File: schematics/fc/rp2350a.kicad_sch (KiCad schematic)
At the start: 53 parts, among them Q1 DMN1150UFB-7B, Q2 DMN1150UFB-7B, Q3 DMN1150UFB-7B, U2 TS2306A 240GF MSM 9_C2976675, U3 RP2354B_C39843328, X1 XTM25012000JT00351001

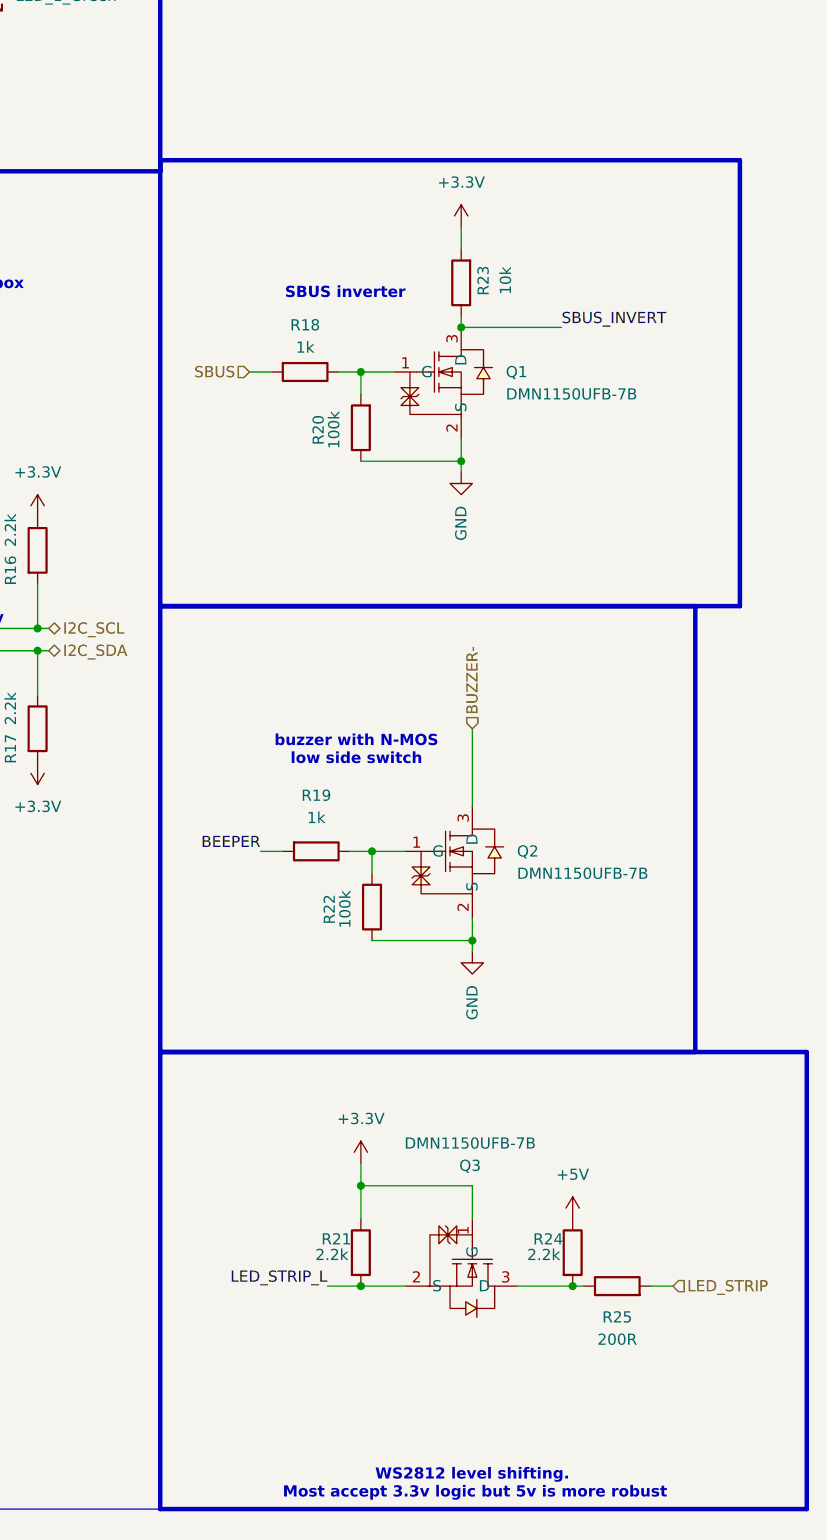
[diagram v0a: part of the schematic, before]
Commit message: checkpoint: Bluejay/BLHeli_S part imports + ESC rework notes
EFM8BB51F16G (C6547511), AGM310MAP (C5184858), BY25Q64ESCIG (C50176394)
imported into libs/lib.kicad_sym + lib.pretty + lib.3dshapes.
BLHELI_S_ESC_NOTES.md documents gate-drive research (1S direct drive vs
2S level-shift requirement) and open design decisions.

Co-Authored-By: Claude Fable 5 <noreply@anthropic.com>
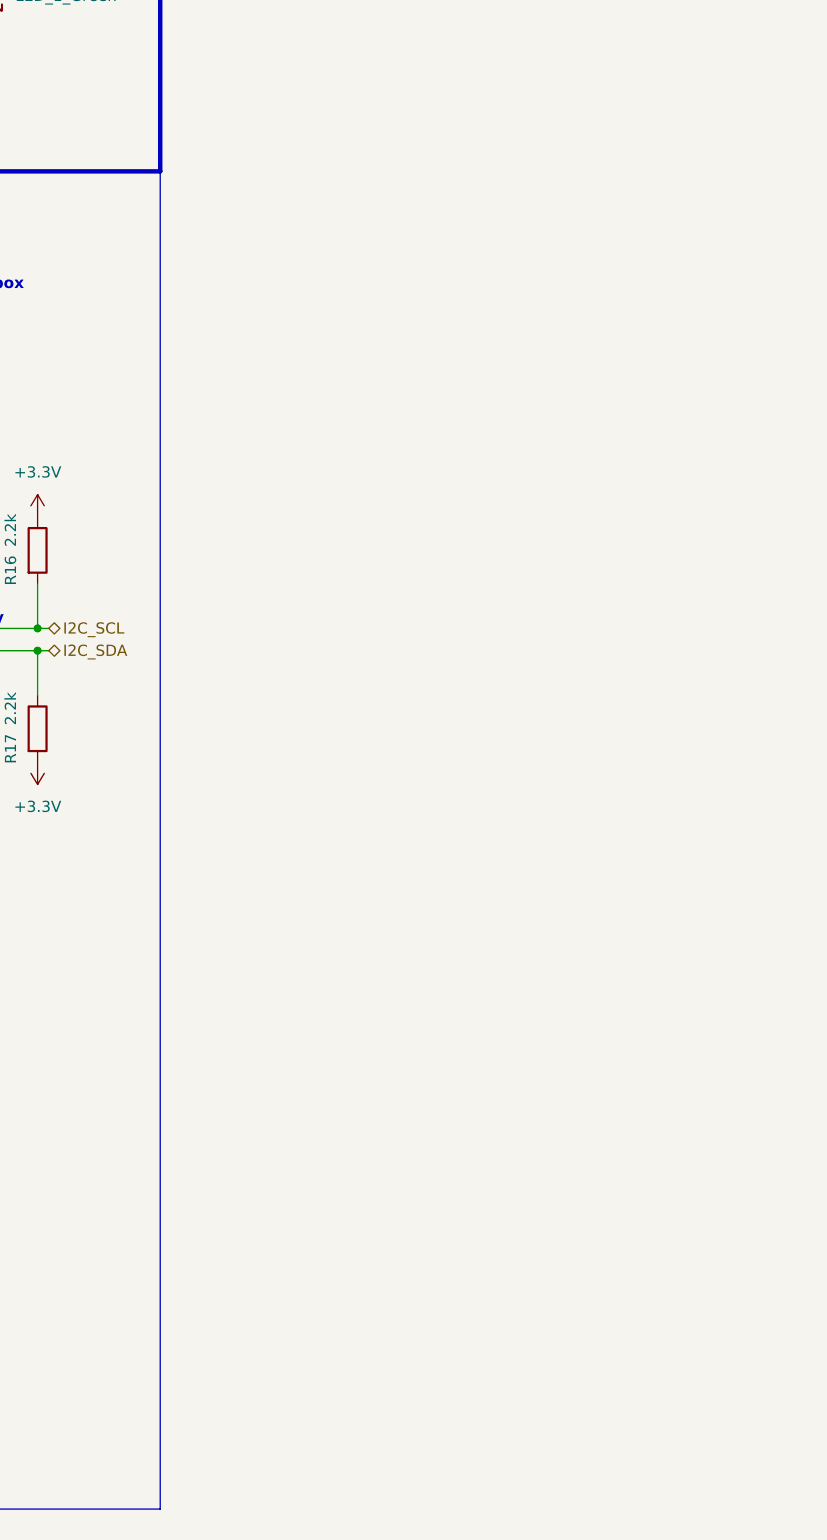
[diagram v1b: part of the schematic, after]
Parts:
- removed Q1, Q2, Q3: DMN1150UFB-7B, lib:DFN-3L_L1.0-W0.6-P0.65-BR, symbol lib:DMN1150UFB-7B
- removed R18, R19: 1k, Resistor_SMD:R_0201_0603Metric, symbol Device:R
- removed R20, R22: 100k, Resistor_SMD:R_0201_0603Metric, symbol Device:R
- removed R21, R24: 2.2k, Resistor_SMD:R_0201_0603Metric, symbol Device:R
- removed R23: 10k, Resistor_SMD:R_0201_0603Metric, symbol Device:R
- removed R25: 200R, Resistor_SMD:R_0201_0603Metric, symbol Device:R
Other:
- note removed: "SBUS inverter"
- note removed: "WS2812 level shifting. Most accept 3.3v logic but 5v is more robust"
- note removed: "buzzer with N-MOS low side switch"
